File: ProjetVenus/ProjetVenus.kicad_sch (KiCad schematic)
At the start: 42 parts, among them J1 Conn_01x02_Pin, J2 Conn_01x04_Pin, J4 Conn_01x02_Pin, J5 Conn_01x05_Pin, Q1 Q_NMOS_DSG, U1 ATtiny412-SS, U2 ADP2108AUJZ-3.0-R7, U3 MS5607-02BA

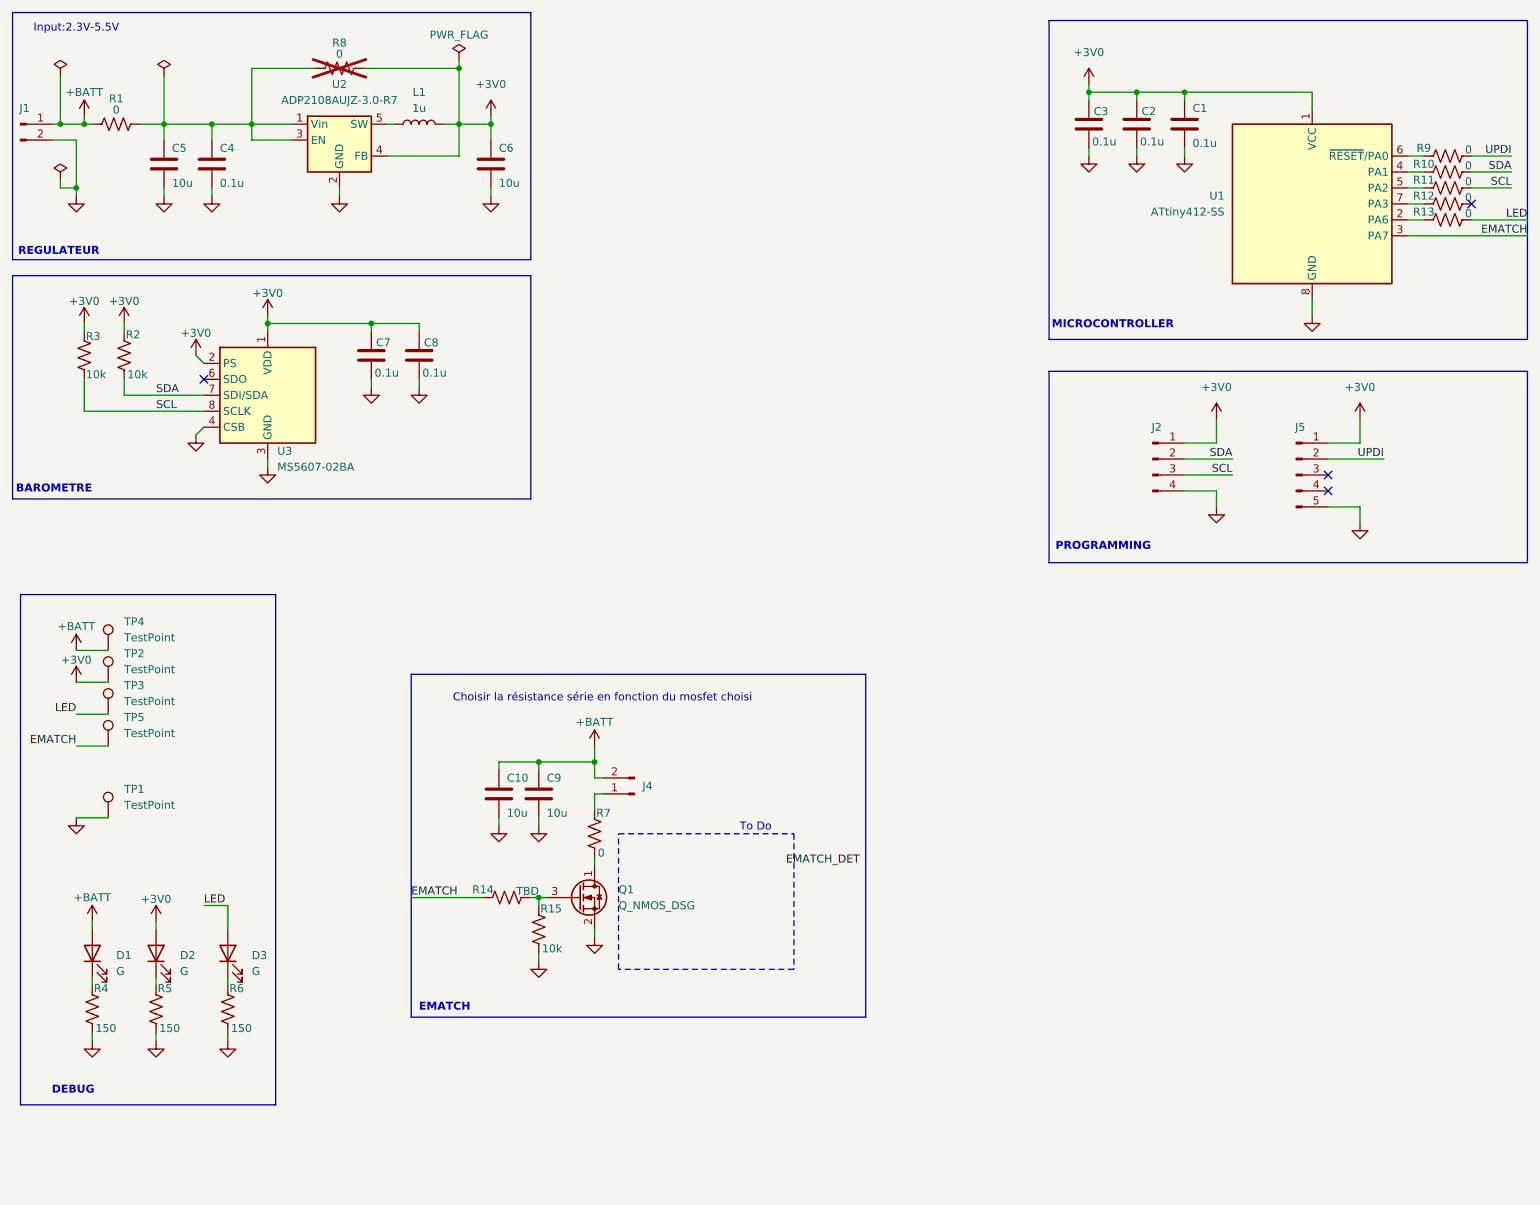
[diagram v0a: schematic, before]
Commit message: V1.0
La chip U3 a du cosmétiques qui va disparaitre a moins qu'on change le footprint, mais on s'en fou un peu
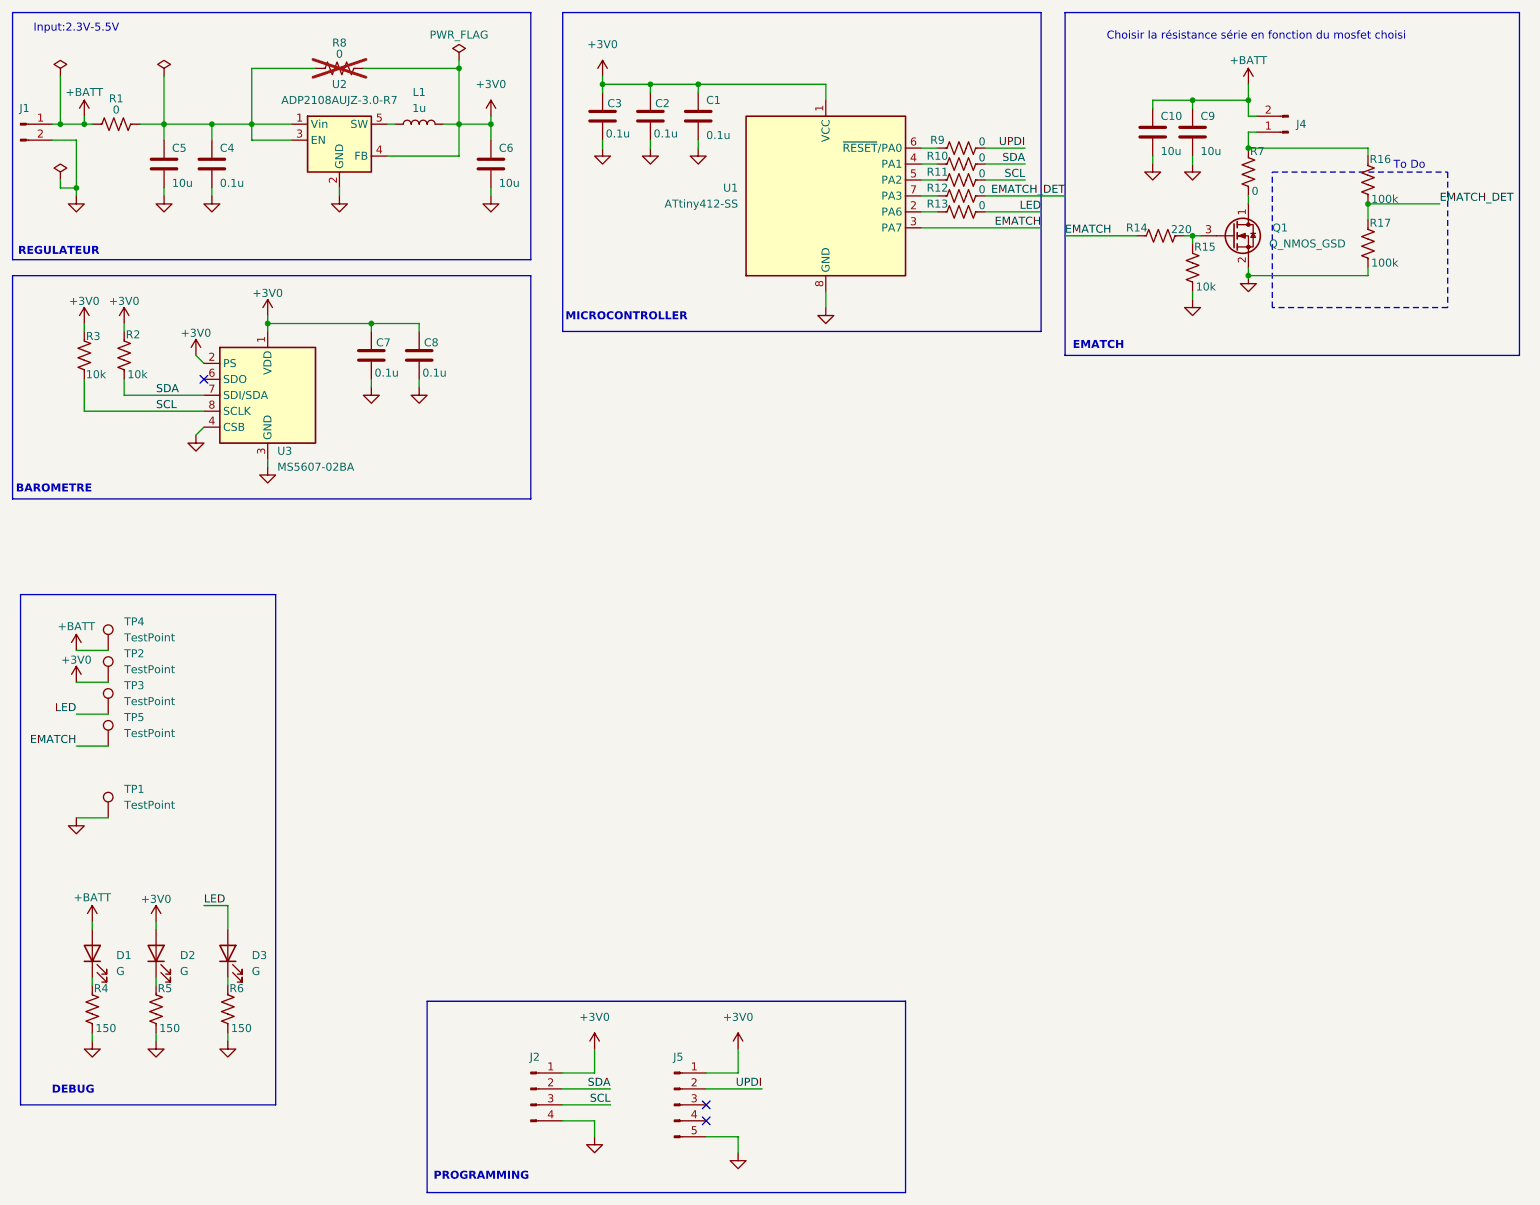
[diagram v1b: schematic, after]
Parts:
- added R16, R17: 100k, Resistor_SMD:R_0603_1608Metric, symbol Device:R_US
- Q1: value Q_NMOS_DSG -> Q_NMOS_GSD; footprint (none) -> Package_TO_SOT_SMD:SOT-23
- R14: value TBD -> 220
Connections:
- net EMATCH_DET: now also R12.2, R16.1, R17.2
- net GND: now also R17.1
- net at J4.1 (Pin_1), R7.2: now also R16.2
- no-connect marks 4 -> 3
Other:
- moved on the sheet: C1, C10, C2, C3, C9, J2, J4, J5, Q1, R10, R11, R12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

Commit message: V1.1
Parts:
- added H1, H2, H3, H4: MountingHole, MountingHole:MountingHole_3.2mm_M3_Pad_Via, symbol Mechanical:MountingHole

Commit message: V1.2
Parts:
- removed H1, H2, H3, H4: MountingHole, MountingHole:MountingHole_3.2mm_M3_Pad_Via, symbol Mechanical:MountingHole
- added H1, H2, H3, H4: MountingHole_Pad, MountingHole:MountingHole_3.2mm_M3_DIN965_Pad, symbol Mechanical:MountingHole_Pad
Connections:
- no-connect marks 3 -> 7
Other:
- moved on the sheet: C10, C9, J4
